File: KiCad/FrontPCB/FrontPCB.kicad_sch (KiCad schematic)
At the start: 18 parts, among them U1 ESP32-S3-WROOM-1

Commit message: CHG: changed wiring of front PCB
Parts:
- removed C1, C3, C5, C7: 0.1µF, Capacitor_SMD:C_0805_2012Metric, symbol Device:C
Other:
- moved on the sheet: C2, C4, C6, C8, D1, D2, D3, D4, D5, D6, D7, D8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

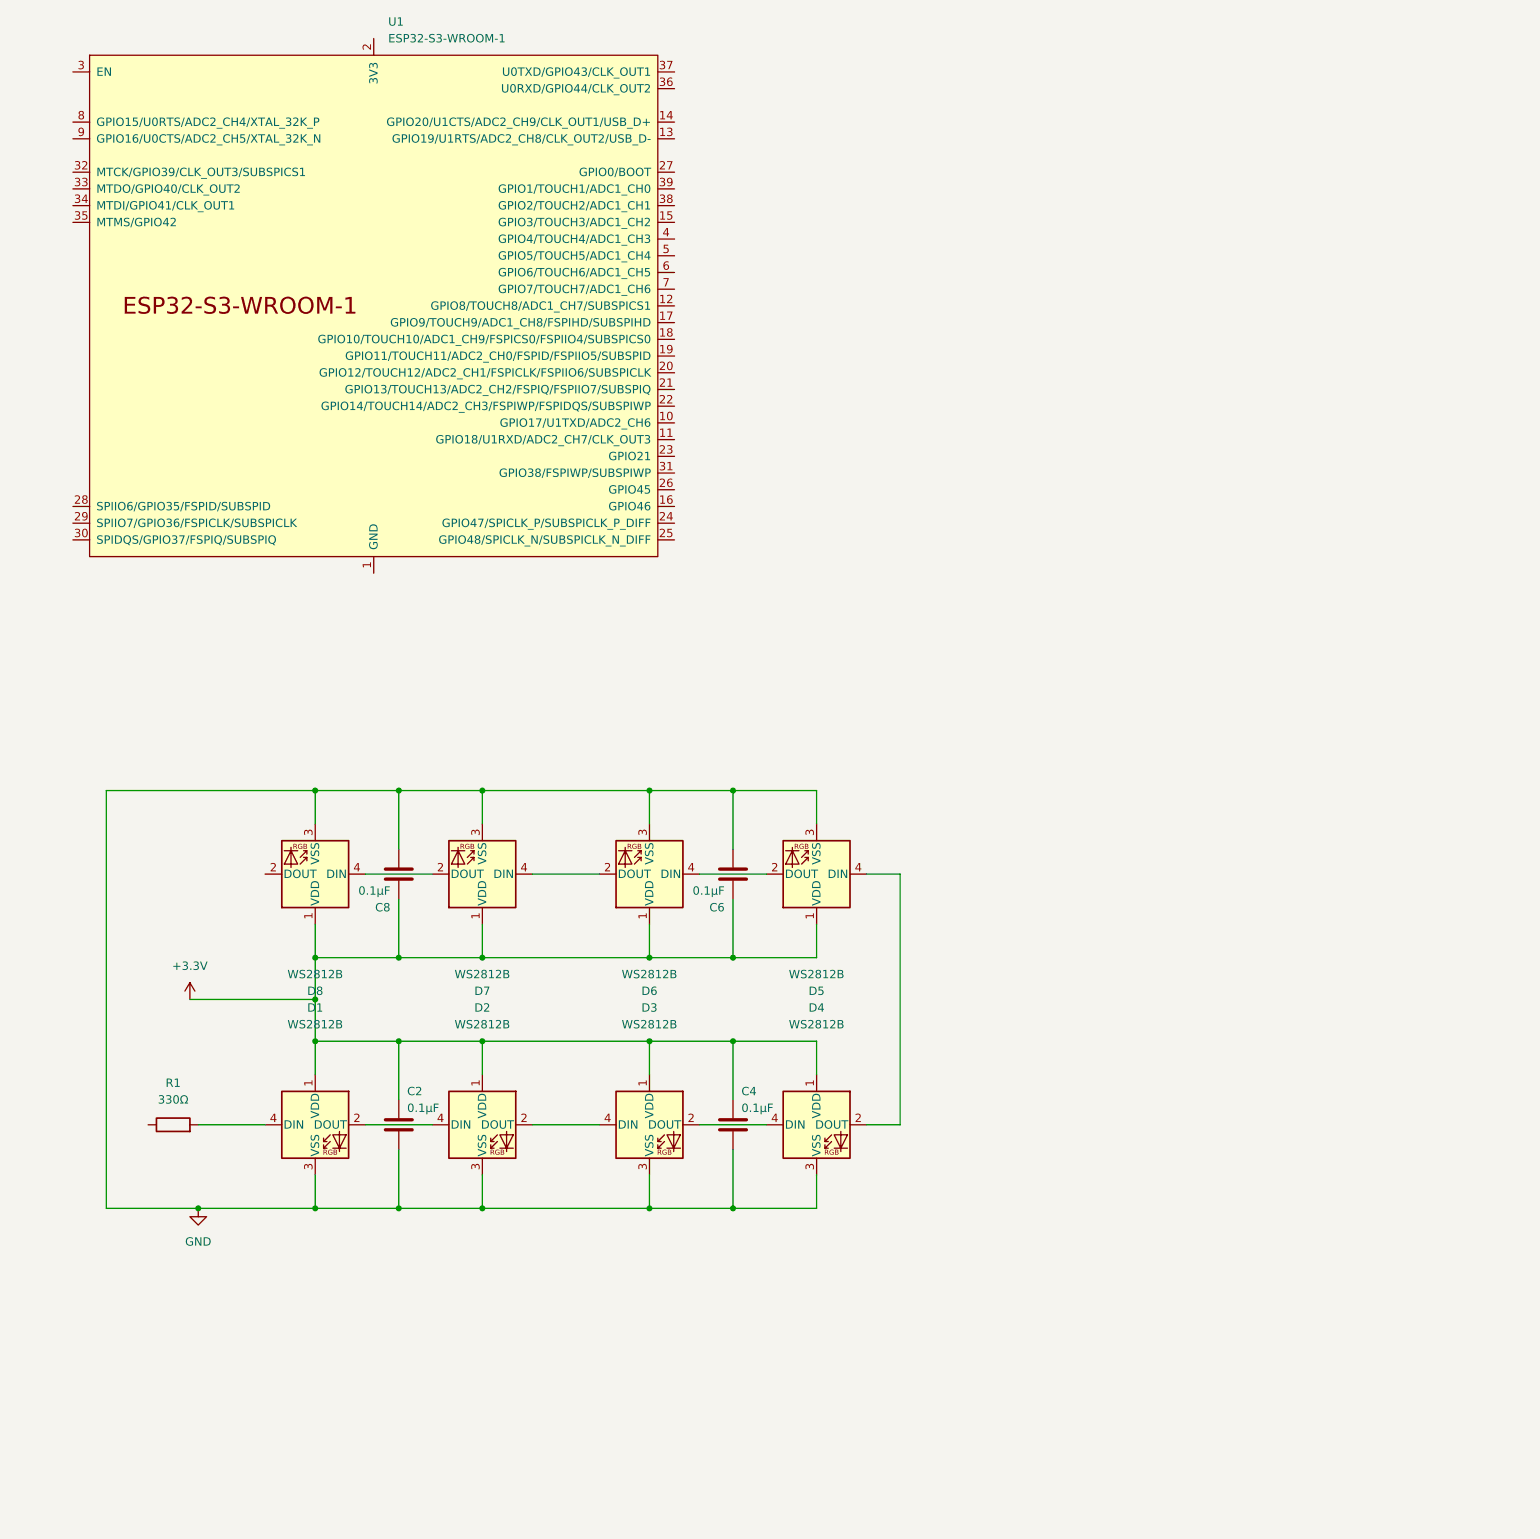
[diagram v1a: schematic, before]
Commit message: CHG: components of FrontPCB added
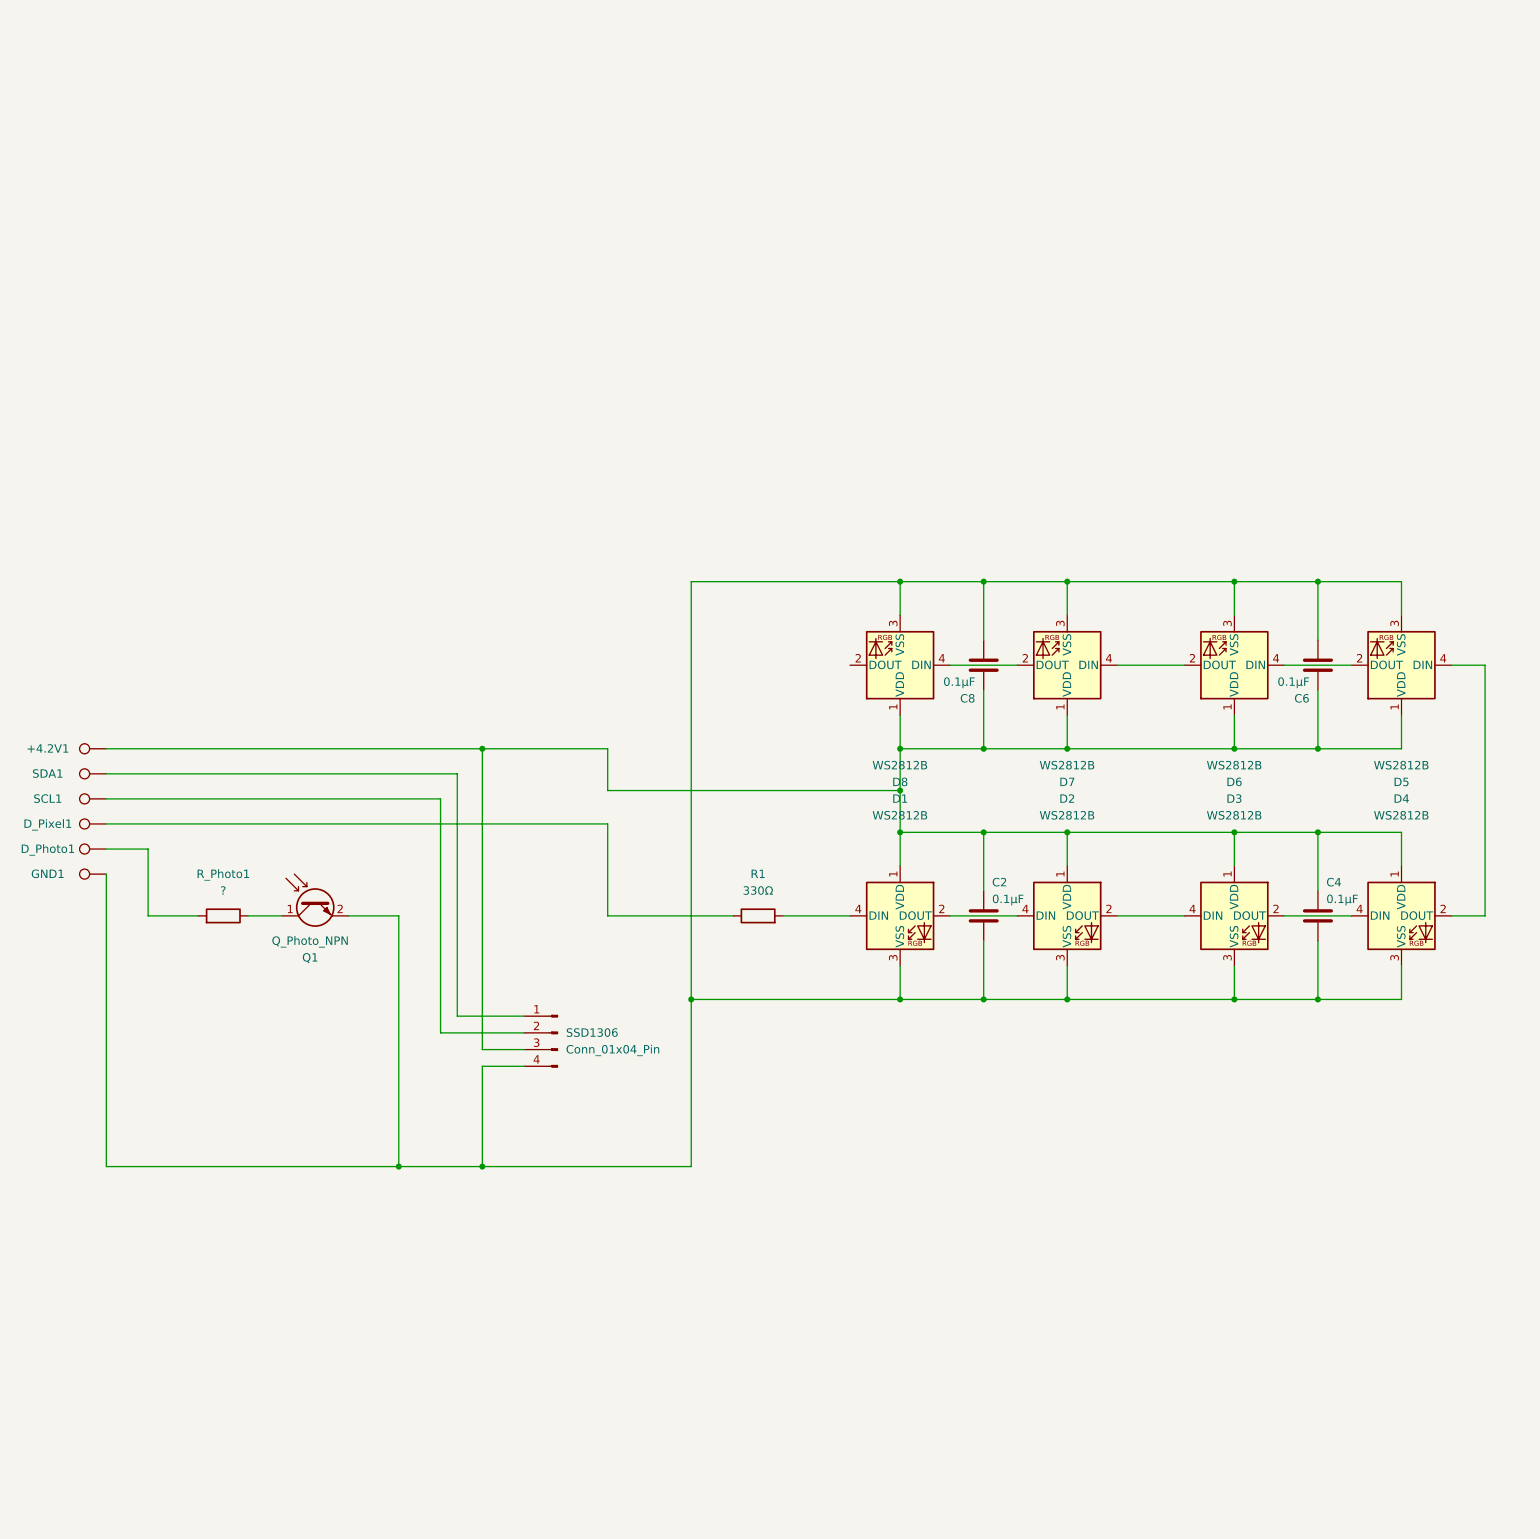
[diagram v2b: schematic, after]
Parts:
- removed U1: ESP32-S3-WROOM-1, PCM_Espressif:ESP32-S3-WROOM-1, symbol PCM_Espressif:ESP32-S3-WROOM-1
- added +4.2V1, D_Photo1, D_Pixel1, GND1, SCL1, SDA1: TestPoint, TestPoint:TestPoint_Pad_2.0x2.0mm, symbol Connector:TestPoint
- added Q1: Q_Photo_NPN, LED_SMD:LED_0805_2012Metric, symbol Device:Q_Photo_NPN
- added R_Photo1: ?, Resistor_SMD:R_0805_2012Metric, symbol Device:R
- added SSD1306: Conn_01x04_Pin, Connector_PinHeader_2.54mm:PinHeader_1x04_P2.54mm_Vertical_SMD_Pin1Left, symbol Connector:Conn_01x04_Pin
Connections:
- net at R1.1: now also D_Pixel1.1
- net +3.3V: no longer names the net of C2.1, C4.1, C6.1, C8.1, D1.1 (VDD), D2.1 (VDD), D3.1 (VDD), D4.1 (VDD), D5.1 (VDD), D6.1 (VDD), D7.1 (VDD), D8.1 (VDD)
- net +3.3V: now also +4.2V1.1, SSD1306.3 (Pin_3)
- net GND: no longer names the net of C2.2, C4.2, C6.2, C8.2, D1.3 (VSS), D2.3 (VSS), D3.3 (VSS), D4.3 (VSS), D5.3 (VSS), D6.3 (VSS), D7.3 (VSS), D8.3 (VSS)
- net GND: now also GND1.1, Q1.2 (E), SSD1306.4 (Pin_4)
- new net: Q1.1 (C), R_Photo1.1
- new net: D_Photo1.1, R_Photo1.2
- new net: SDA1.1, SSD1306.1 (Pin_1)
- new net: SCL1.1, SSD1306.2 (Pin_2)
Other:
- moved on the sheet: C2, C4, C6, C8, D1, D2, D3, D4, D5, D6, D7, D8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
